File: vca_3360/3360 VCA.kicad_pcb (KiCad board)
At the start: 2 copper layers, 100 x 56 mm, 55 parts, among them J1 Power in, J2 Input1, J3 CV1 In, J4 Input2, J5 CV2 In, J6 LED1, J7 LED2, J8 OUTPUT1, J9 OUTPUT2, Q1 2N3904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

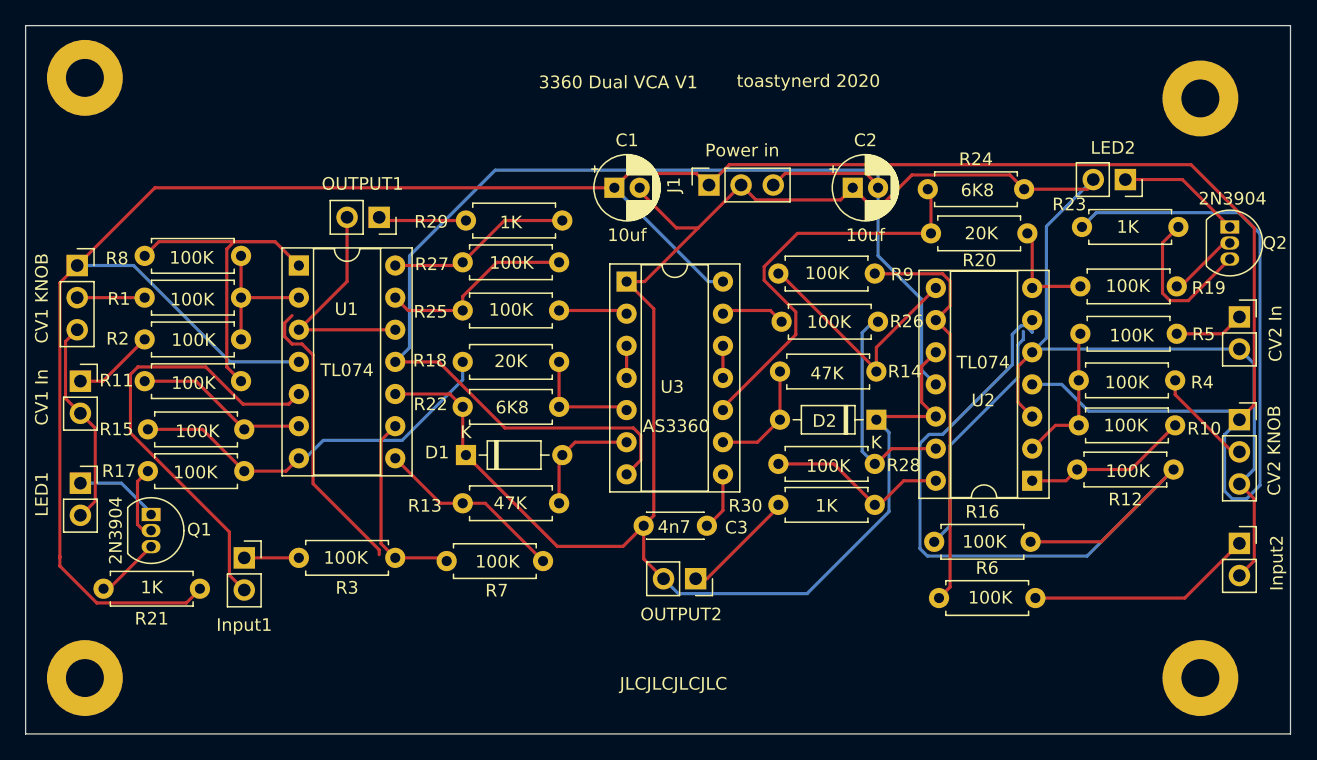
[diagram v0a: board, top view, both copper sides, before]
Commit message: attenuverter and 3340 schematics
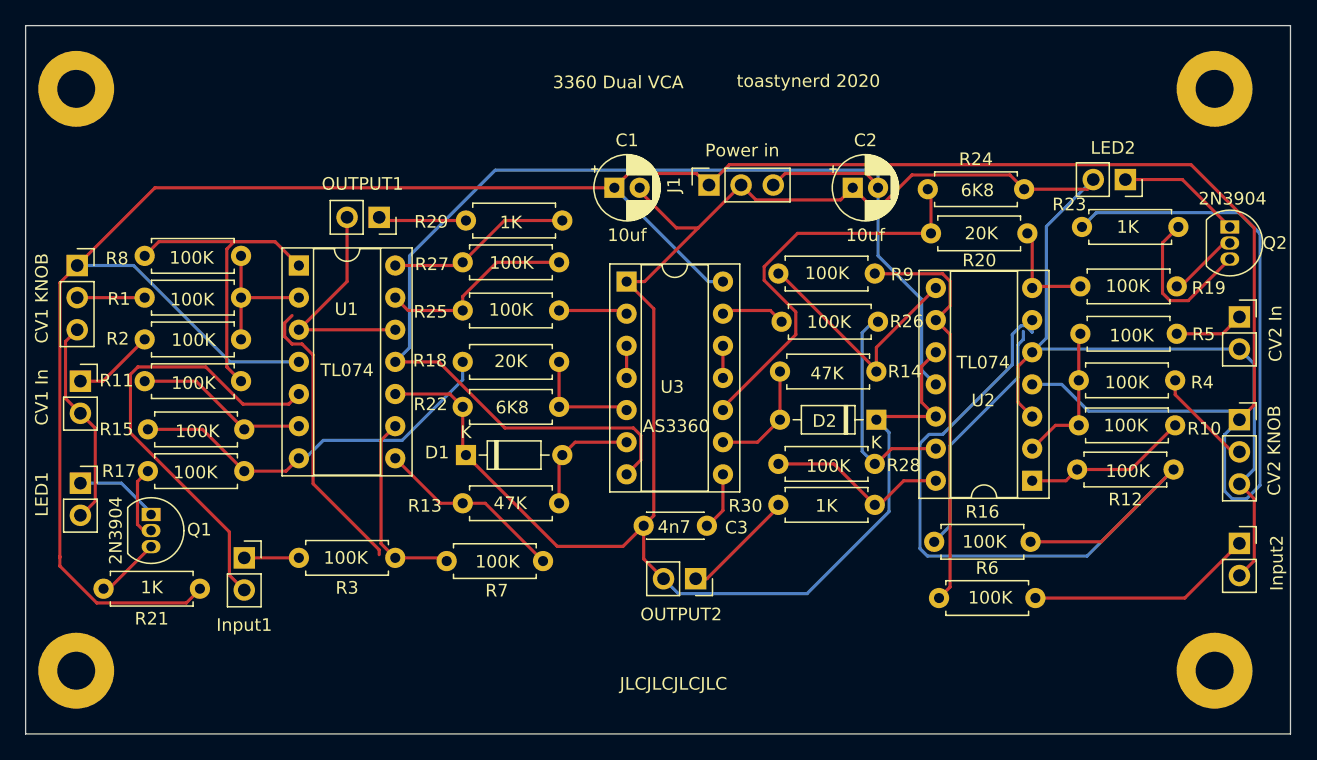
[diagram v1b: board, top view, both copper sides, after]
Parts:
- moved ? 1.36 mm to (206.0, 95.0)
- moved ? 1.26 mm to (206.0, 141.0)
- moved ? 1.11 mm to (116.0, 95.0)
- moved ? 0.90 mm to (116.0, 141.0)
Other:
- board text added: "3360 Dual VCA"
- board text removed: "3360 Dual VCA V1"
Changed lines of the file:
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@@
       (outputformat 1)
       (mirror false)
-      (drillshape 1)
+      (drillshape 0)
       (scaleselection 1)
-      (outputdirectory ""))
+      (outputdirectory "/Users/toasty/electronics/synth_schematics/vca_3360/gerber/"))
   )
   (net 0 "")
@@
   )
   (module MountingHole:MountingHole_3mm_Pad (layer F.Cu)
-    (at 204.8764 95.758)
+    (at 206 95)
     (descr "Mounting Hole 3mm")
     (tags "mounting hole 3mm")
@@
   )
   (module MountingHole:MountingHole_3mm_Pad (layer F.Cu)
-    (at 204.8764 141.5796)
+    (at 206 141)
     (descr "Mounting Hole 3mm")
     (tags "mounting hole 3mm")
@@
   )
   (module MountingHole:MountingHole_3mm_Pad (layer F.Cu)
-    (at 116.6876 141.5796)
+    (at 116 141)
     (descr "Mounting Hole 3mm")
     (tags "mounting hole 3mm")
@@
   )
   (module MountingHole:MountingHole_3mm_Pad (layer F.Cu)
-    (at 116.6876 94.1324)
+    (at 116 95)
     (descr "Mounting Hole 3mm")
     (tags "mounting hole 3mm")
@@
       (effects (font (size 1 1) (thickness 0.15)))
     )
-    (fp_text value BZX55C2V0 (at 3.81 2.12) (layer F.Fab) hide
+    (fp_text value BZX55C2V0 (at 3.81 2.12) (layer F.Fab)
       (effects (font (size 1 1) (thickness 0.15)))
     )
@@
       (effects (font (size 1 1) (thickness 0.15)))
     )
-    (fp_text value BZX55C2V0 (at 3.81 2.12) (layer F.Fab) hide
+    (fp_text value BZX55C2V0 (at 3.81 2.12) (layer F.Fab)
       (effects (font (size 1 1) (thickness 0.15)))
     )
@@
     (effects (font (size 1 1) (thickness 0.15)))
   )
-  (gr_text "3360 Dual VCA V1\n" (at 158.8516 94.488) (layer F.SilkS)
+  (gr_text "3360 Dual VCA\n" (at 158.8516 94.488) (layer F.SilkS)
     (effects (font (size 1 1) (thickness 0.15)))
   )

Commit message: 3360 stencil and 3340 fixes
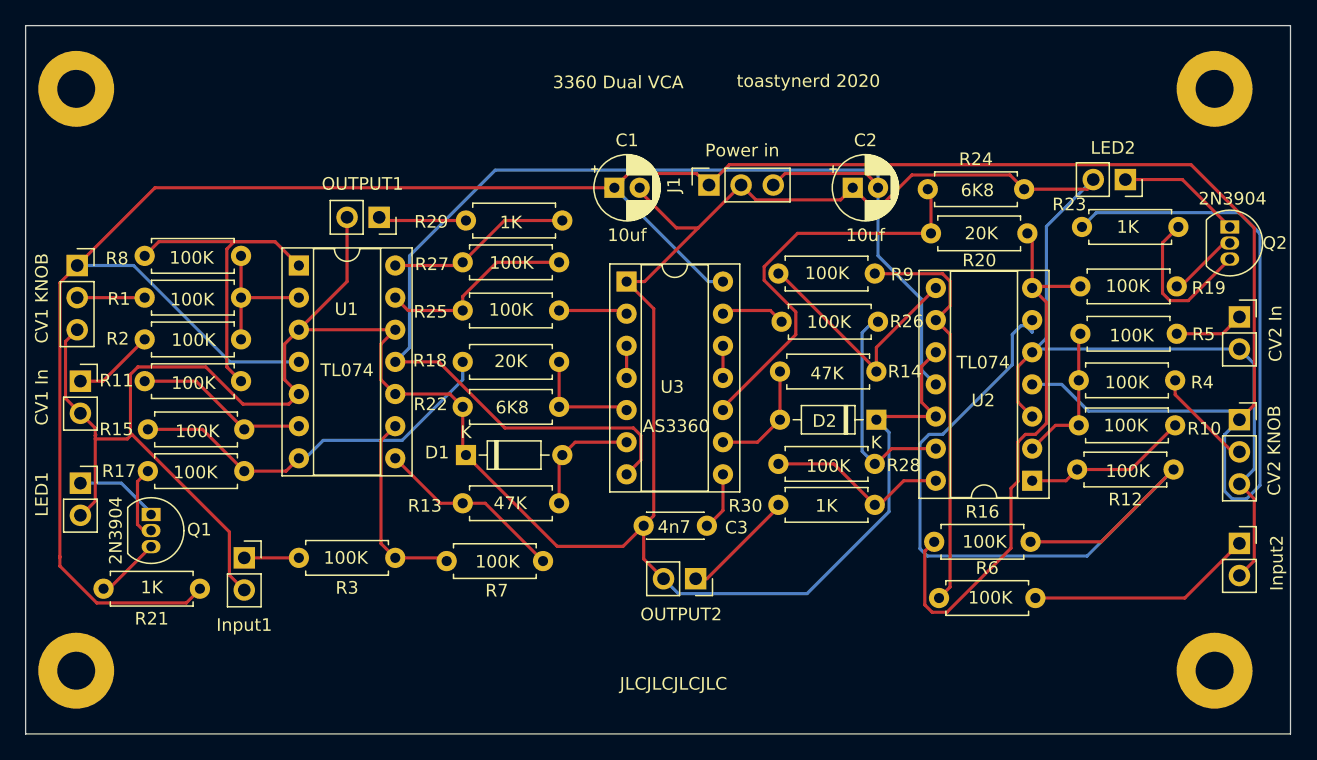
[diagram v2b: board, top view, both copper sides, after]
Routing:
- net (no net): track 22.7 -> 0.00 mm
- net Net-(R16-Pad1): track 28.1 -> 45.7 mm
- net GND: track 273.0 -> 288.6 mm
